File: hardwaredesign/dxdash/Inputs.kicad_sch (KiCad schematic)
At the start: 10 parts, among them J9 Temps

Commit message: controller board added features
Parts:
- removed C61 (x3): 100nF, Capacitor_SMD:C_1206_3216Metric_Pad1.33x1.80mm_HandSolder, symbol Device:C_Small
- removed J9: Temps, Connector_PinHeader_2.54mm:PinHeader_1x04_P2.54mm_Vertical, symbol Connector:Conn_01x04_Pin
- removed R11 (x3): 47k, Resistor_SMD:R_1206_3216Metric_Pad1.30x1.75mm_HandSolder, symbol Device:R_Small
- removed R11 (x3): 10k, Resistor_SMD:R_1206_3216Metric_Pad1.30x1.75mm_HandSolder, symbol Device:R_Small
- added C2, C3: 100nF, Capacitor_SMD:C_1206_3216Metric_Pad1.33x1.80mm_HandSolder, symbol Device:C_Small
- added J2: Conn_01x06_Pin, Connector_PinHeader_2.54mm:PinHeader_1x06_P2.54mm_Vertical, symbol Connector:Conn_01x06_Pin
- added R1, R13, R3, R5: 10k, Resistor_SMD:R_1206_3216Metric_Pad1.30x1.75mm_HandSolder, symbol Device:R_Small
- added R14, R16, R25, R26, R27, R28, R39, R40: 47k, Resistor_SMD:R_1206_3216Metric_Pad1.30x1.75mm_HandSolder, symbol Device:R_Small
- added R41: 100, Resistor_SMD:R_1206_3216Metric_Pad1.30x1.75mm_HandSolder, symbol Device:R_Small
- added SW2, SW3, SW4, SW5: SW_Push, Button_Switch_THT:SW_PUSH_6mm_H5mm, symbol Switch:SW_Push
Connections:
- net 3V3_uC: now also R1.1, R13.1, R3.1, R5.1
- net GND: now also C2.2, C3.2, J2.5 (Pin_5), J2.6 (Pin_6), R28.1, R40.1, SW2.1, SW3.1, SW4.1, SW5.1
- new net: R1.2, R26.1, SW2.2
- new net: J2.3 (Pin_3), R27.1
- new net: R13.2, R14.1, SW5.2
- new net: R16.1, R5.2, SW4.2
- new net: J2.1 (Pin_1), J2.2 (Pin_2), R41.1
- new net: J2.4 (Pin_4), R39.1
- new net: R25.1, R3.2, SW3.2
- new net 5V: R41.2
- new net uC_button1: R26.2
- new net uC_button2: R25.2
- new net uC_button3: R16.2
- new net uC_button4: R14.2
- new net uC_pot1: C3.1, R27.2, R28.2
- new net uC_pot2: C2.1, R39.2, R40.2
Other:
- note added: "dual poti inputs (0 to 5V)"
- note removed: "Analog inputs, e.g. for use with NTCs to ground for temperature measurement or analog feedback contacts or switches."
- note removed: "todo: poti inputs (0 to 5V)"

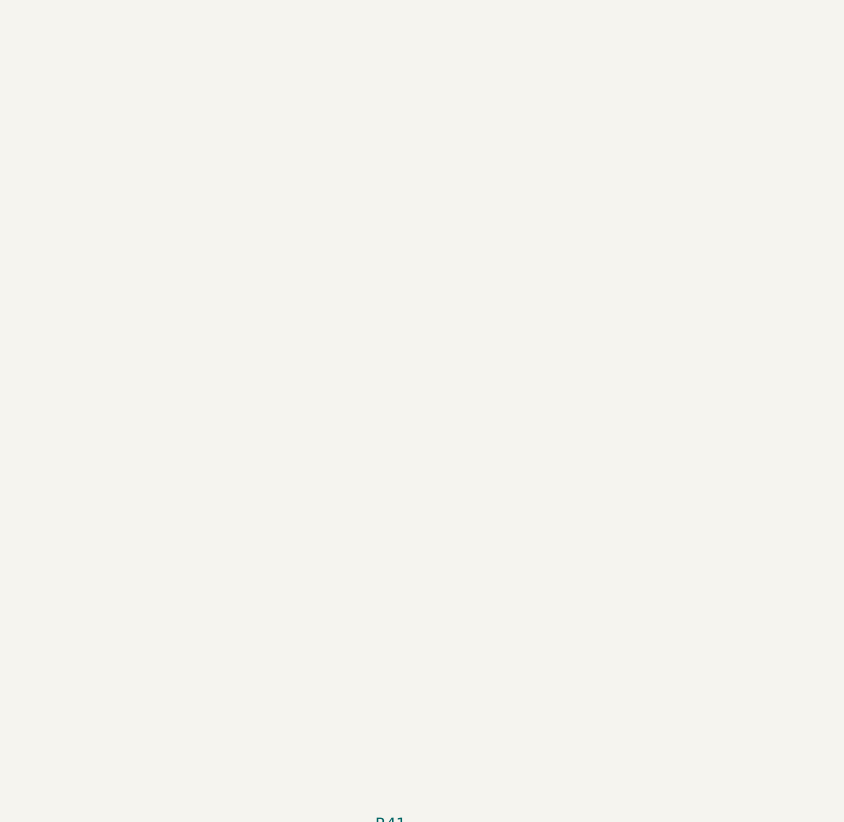
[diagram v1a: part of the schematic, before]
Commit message: added joystick
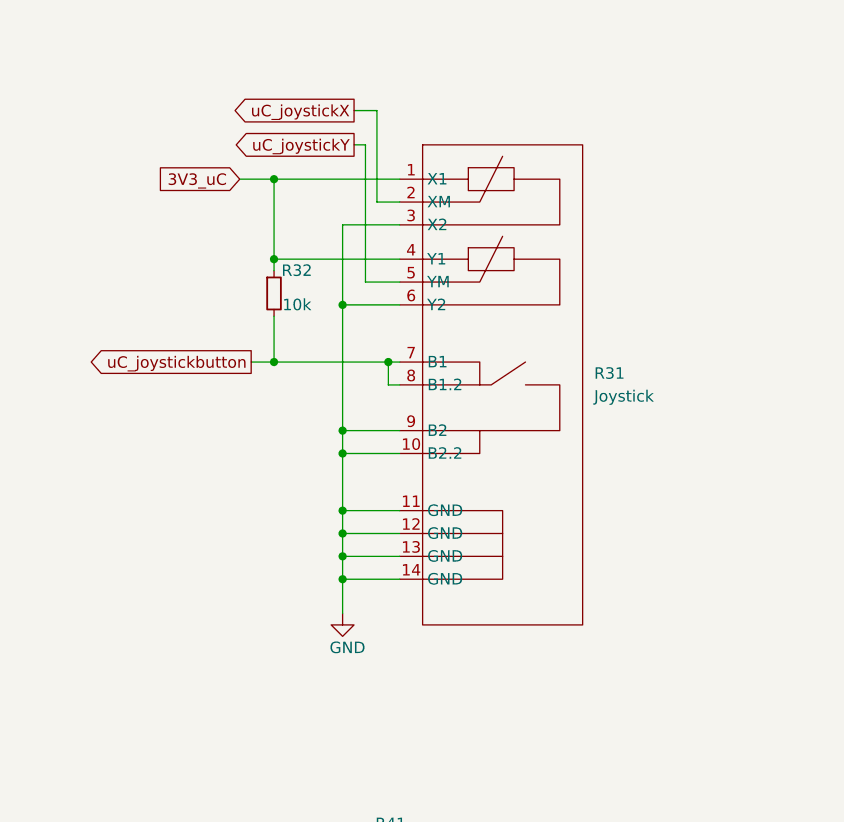
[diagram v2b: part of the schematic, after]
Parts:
- added R31: Joystick, libJoystick:joystickXYButton, symbol libJoystick:joystickXYButton
- added R32: 10k, Resistor_SMD:R_1206_3216Metric_Pad1.30x1.75mm_HandSolder, symbol Device:R_Small
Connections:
- net 3V3_uC: now also R31.1 (X1), R31.4 (Y1), R32.1
- net GND: now also R31.10 (B2.2), R31.11 (GND), R31.12 (GND), R31.13 (GND), R31.14 (GND), R31.3 (X2), R31.6 (Y2), R31.9 (B2)
- new net uC_joystickX: R31.2 (XM)
- new net uC_joystickY: R31.5 (YM)
- new net uC_joystickbutton: R31.7 (B1), R31.8 (B1.2), R32.2

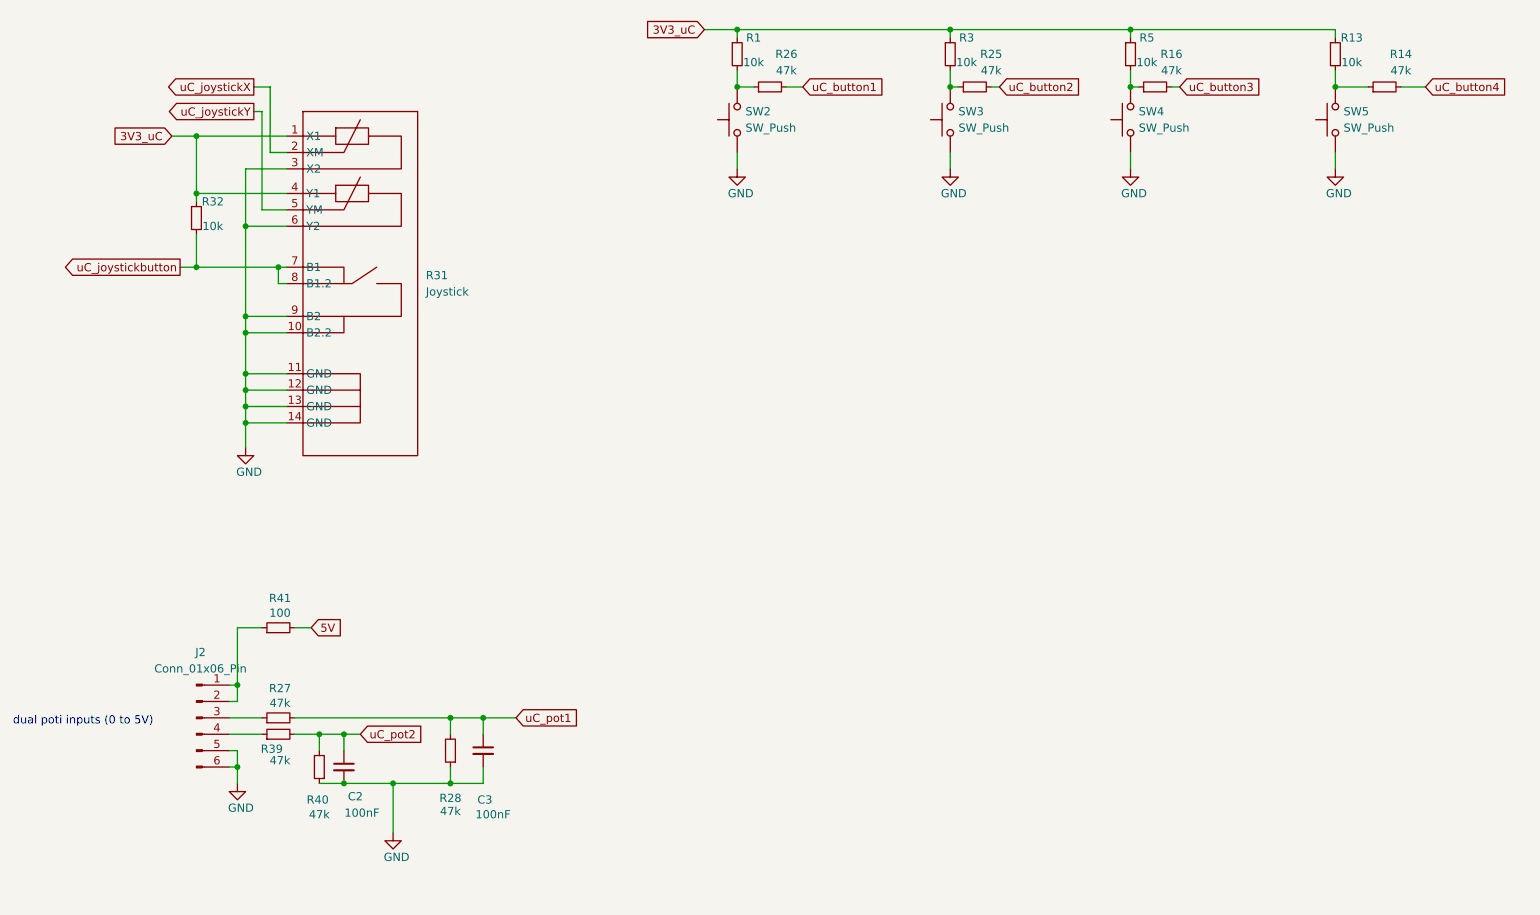
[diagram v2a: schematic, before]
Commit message: added screw terminals
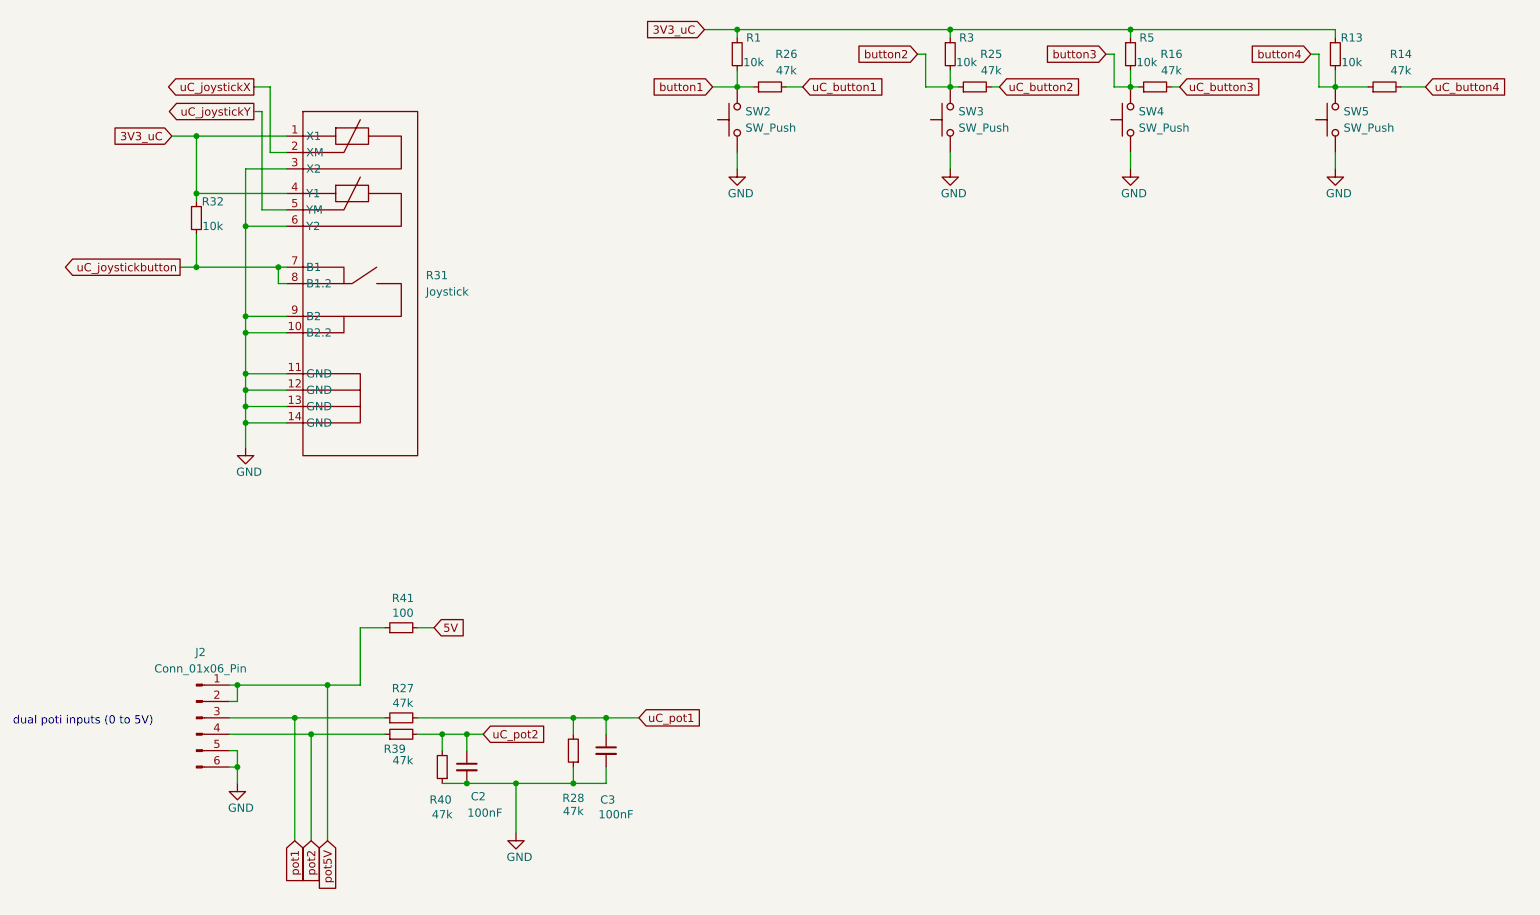
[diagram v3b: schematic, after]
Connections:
- net button1: now reaches R1.2, R26.1, SW2.2
- net pot1: now reaches J2.3 (Pin_3), R27.1
- net button4: now reaches R13.2, R14.1, SW5.2
- net button3: now reaches R16.1, R5.2, SW4.2
- net pot5V: now reaches J2.1 (Pin_1), J2.2 (Pin_2), R41.1
- net pot2: now reaches J2.4 (Pin_4), R39.1
- net button2: now reaches R25.1, R3.2, SW3.2
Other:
- moved on the sheet: C2, C3, R27, R28, R39, R40, R41

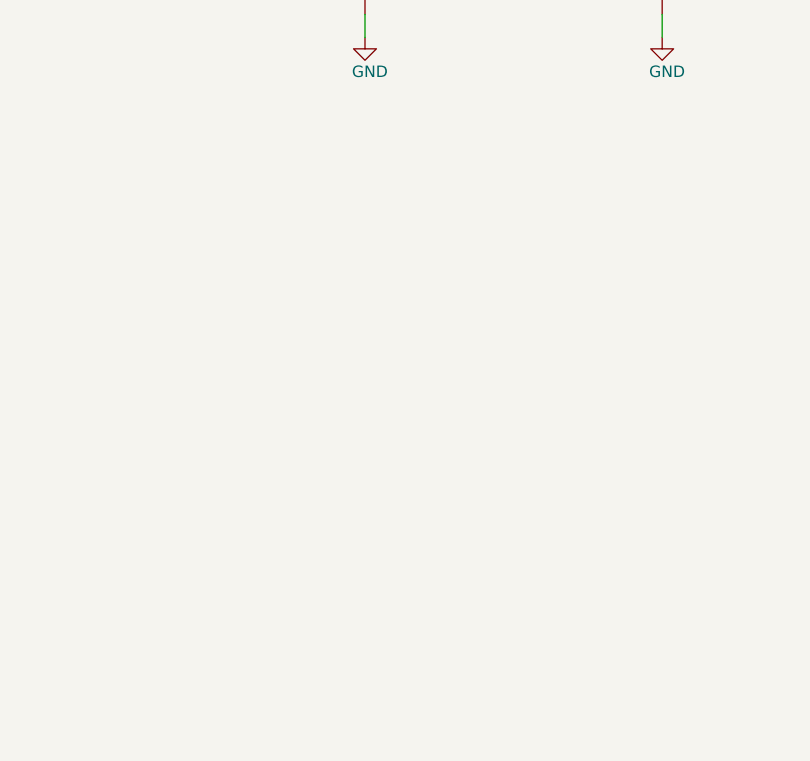
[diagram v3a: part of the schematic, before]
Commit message: added switch inputs. Layout preparation.
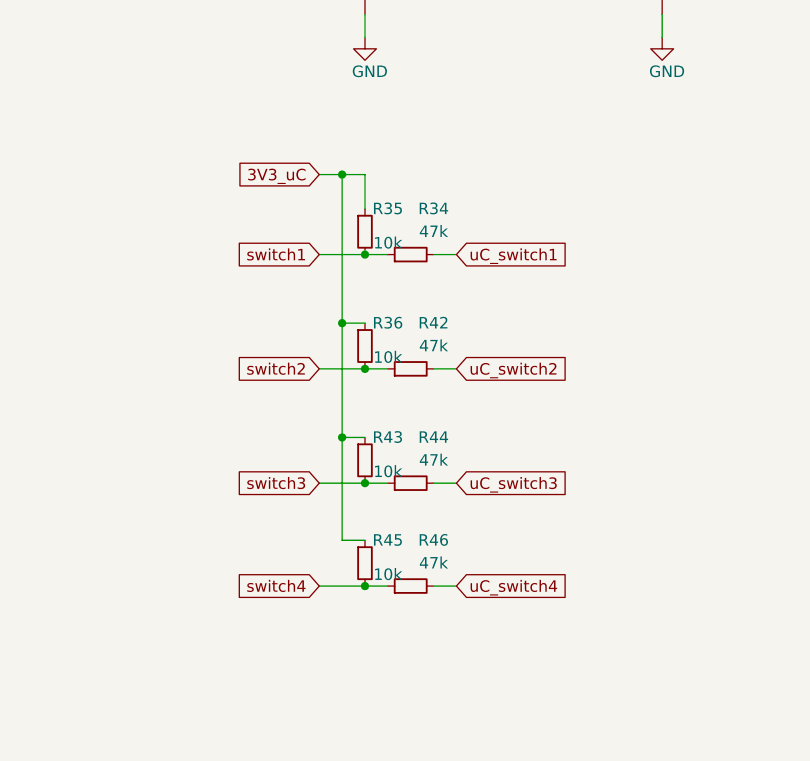
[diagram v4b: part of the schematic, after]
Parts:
- added R34, R42, R44, R46: 47k, Resistor_SMD:R_1206_3216Metric_Pad1.30x1.75mm_HandSolder, symbol Device:R_Small
- added R35, R36, R43, R45: 10k, Resistor_SMD:R_1206_3216Metric_Pad1.30x1.75mm_HandSolder, symbol Device:R_Small
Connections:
- net 3V3_uC: now also R35.1, R36.1, R43.1, R45.1
- new net switch1: R34.1, R35.2
- new net switch2: R36.2, R42.1
- new net switch3: R43.2, R44.1
- new net switch4: R45.2, R46.1
- new net uC_switch1: R34.2
- new net uC_switch2: R42.2
- new net uC_switch3: R44.2
- new net uC_switch4: R46.2

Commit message: more layout
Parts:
- removed J2: Conn_01x06_Pin, Connector_PinHeader_2.54mm:PinHeader_1x06_P2.54mm_Vertical, symbol Connector:Conn_01x06_Pin
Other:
- moved on the sheet: R41
